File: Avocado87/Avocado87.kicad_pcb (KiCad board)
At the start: 2 copper layers, 187 parts, among them U1 proton_c

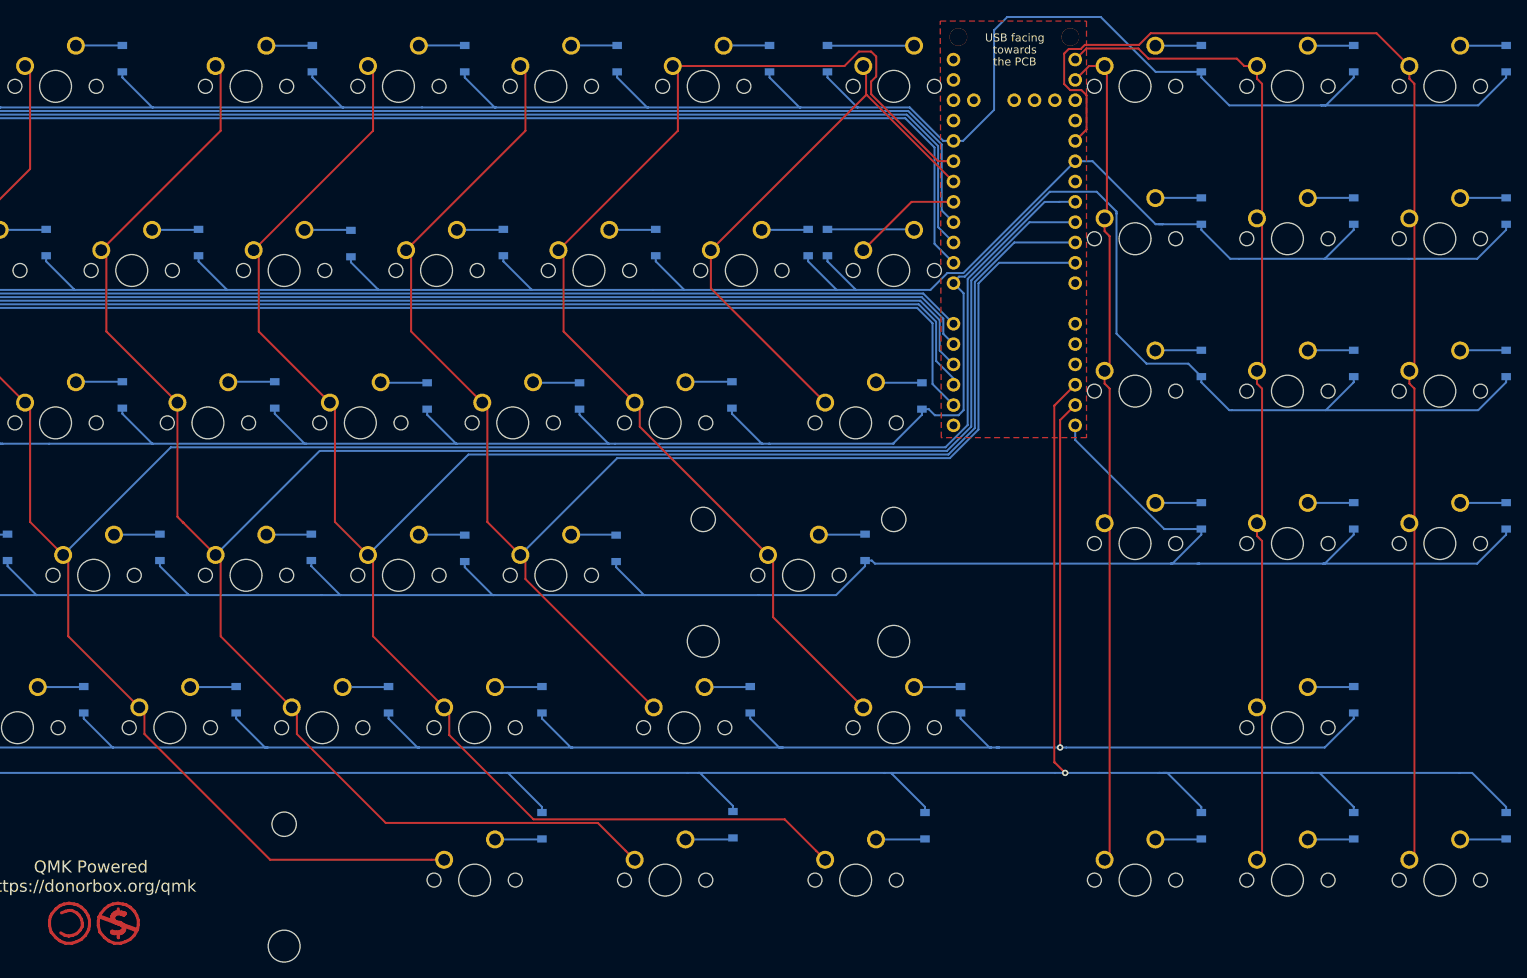
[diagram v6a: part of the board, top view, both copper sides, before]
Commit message: Add i2c and underglow to pcb
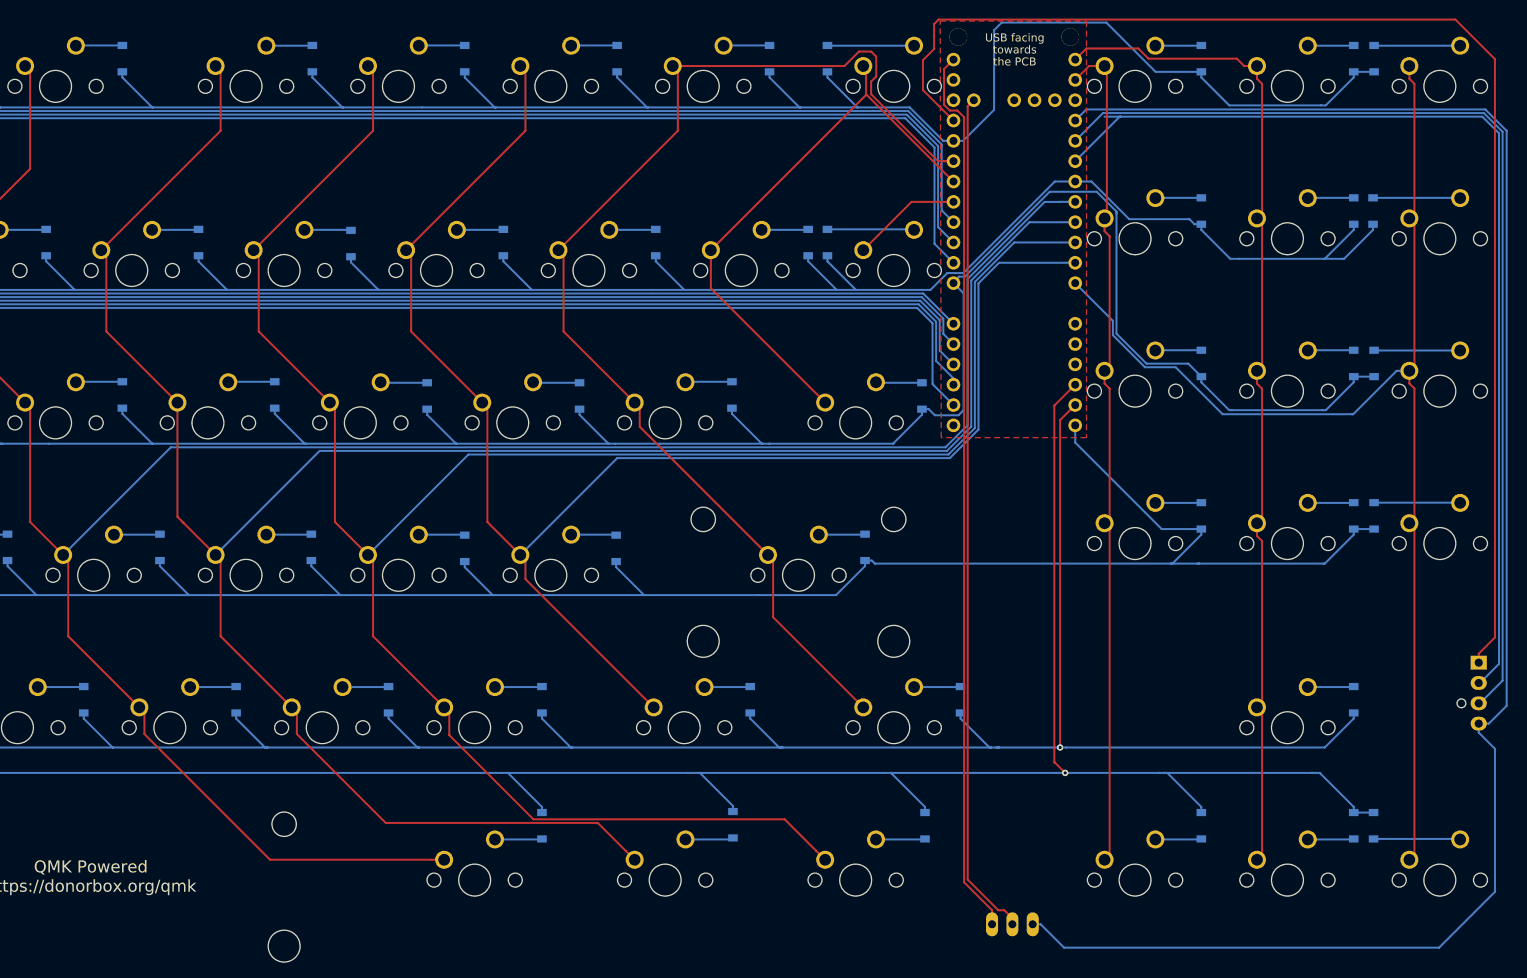
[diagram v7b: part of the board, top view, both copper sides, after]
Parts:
- removed REF**: Symbol_CC-Noncommercial_CopperTop_Small, Symbols:Symbol_CC-Noncommercial_CopperTop_Small
- removed REF**: Symbol_CC-ShareAlike_CopperTop_Small, Symbols:Symbol_CC-ShareAlike_CopperTop_Small
- added I2C1: Conn_01x04_Female, Connectors:Fan_Pin_Header_Straight_1x04, B.Cu at (200.9, 120.5)
- added Underglow: Conn_01x03_Female, Connectors:PINHEAD1-3, B.Cu at (140.1, 153.2)
- D0, D0A1, D0B1, D0C1, D0D1, D0F1, D0G1, D0H1, D1, D10, D11, D12, D13, D14, D15, D16, D17, D18, D19, D1A1, D1B1, D1C1, D1D1, D1E1, D1F1, D1G1, D1H1, D2, D20, D21, D22, D23, D24, D25, D26, D27, D28, D29, D2A1, D2B1, D2C1, D2D1, D2F1, D2G1, D2H1, D3, D30, D31, D32, D33, D34, D35, D36, D37, D38, D39, D3A1, D3B1, D3C1, D3F1, D3G1, D3H1, D4, D40, D41, D42, D43, D44, D45, D46, D47, D48, D49, D4A1, D4B1, D4C1, D4G1, D5, D50, D51, D52, D55, D58, D59, D5A1, D5F1, D5G1, D5H1, D6, D7, D8, D9: footprint Diodes_SMD:D_SOD-123 -> random-keyboard-parts:D_SOD-123-Pretty
- moved D1H1 16.6 mm to (187.7, 64.0)
- moved D5H1 16.6 mm to (187.8, 140.8)
- moved D0H1 16.5 mm to (187.8, 45.0)
- moved D2H1 16.5 mm to (187.8, 83.1)
- moved D3H1 16.5 mm to (187.8, 102.1)
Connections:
- D10 pad 1: B6 -> B5
- D11 pad 1: B6 -> B5
- D12 pad 1: B6 -> B5
- D13 pad 1: B6 -> B5
- D14 pad 1: B6 -> B5
- D15 pad 1: B6 -> B5
- D16 pad 1: B6 -> B5
- D17 pad 1: B6 -> B5
- D18 pad 1: B6 -> B5
- D19 pad 1: B6 -> B5
- D1A1 pad 1: B6 -> B5
- D1B1 pad 1: B6 -> B5
- D1C1 pad 1: B6 -> B5
- D1D1 pad 1: B6 -> B5
- D1E1 pad 1: B6 -> B5
- D1F1 pad 1: B6 -> B5
- D1G1 pad 1: B6 -> B5
- D1H1 pad 1: B6 -> B5
- MX0H1 pad 1: B7 -> B0
- MX1H1 pad 1: B7 -> B0
- MX2H1 pad 1: B7 -> B0
- MX3H1 pad 1: B7 -> B0
- MX5H1 pad 1: B7 -> B0
- U1 pad 3.3V: (no net) -> +3V3
- U1 pad 5V: (no net) -> +5V
- U1 pad A3|5v: (no net) -> A3
- U1 pad B0: (no net) -> B0
- U1 pad B5: (no net) -> B5
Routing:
- net B5: track 0.00 -> 420.4 mm
- net B6: track 439.7 -> 128.0 mm
- net GND: track 0.00 -> 215.7 mm
- net +3V3: track 0.00 -> 163.7 mm
- net B0: track 0.00 -> 153.2 mm
- net +5V: track 0.00 -> 111.6 mm
- net A3: track 0.00 -> 106.1 mm
- net B7: track 160.7 -> 128.6 mm
- net A2: track 444.0 -> 420.7 mm
- net A7: track 441.0 -> 417.8 mm
- net A15: track 433.2 -> 410.9 mm
- net B9: track 460.8 -> 438.7 mm
- net Net-(D1H1-Pad2): track 5.76 -> 10.9 mm
- net Net-(D3H1-Pad2): track 5.76 -> 10.9 mm
- net Net-(D5H1-Pad2): track 5.77 -> 10.9 mm
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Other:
- board text added: "3.3V"
- board text added: "5V"
- board text added: "GND"
- board text added: "RGB"
- board text added: "SCL"
- board text added: "SDA"

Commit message: move underglow away from bottom of board
Leave room for the strip
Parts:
- moved Underglow 6.68 mm to (139.8, 146.5)
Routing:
- net A3: track 106.1 -> 99.6 mm
- net +5V: track 111.6 -> 105.4 mm
- net GND: track 215.7 -> 218.7 mm
